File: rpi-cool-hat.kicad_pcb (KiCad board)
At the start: 2 copper layers, 20.3 x 50.8 mm, 3 parts, among them J1 FAN, J2 HAT, J3 RPi

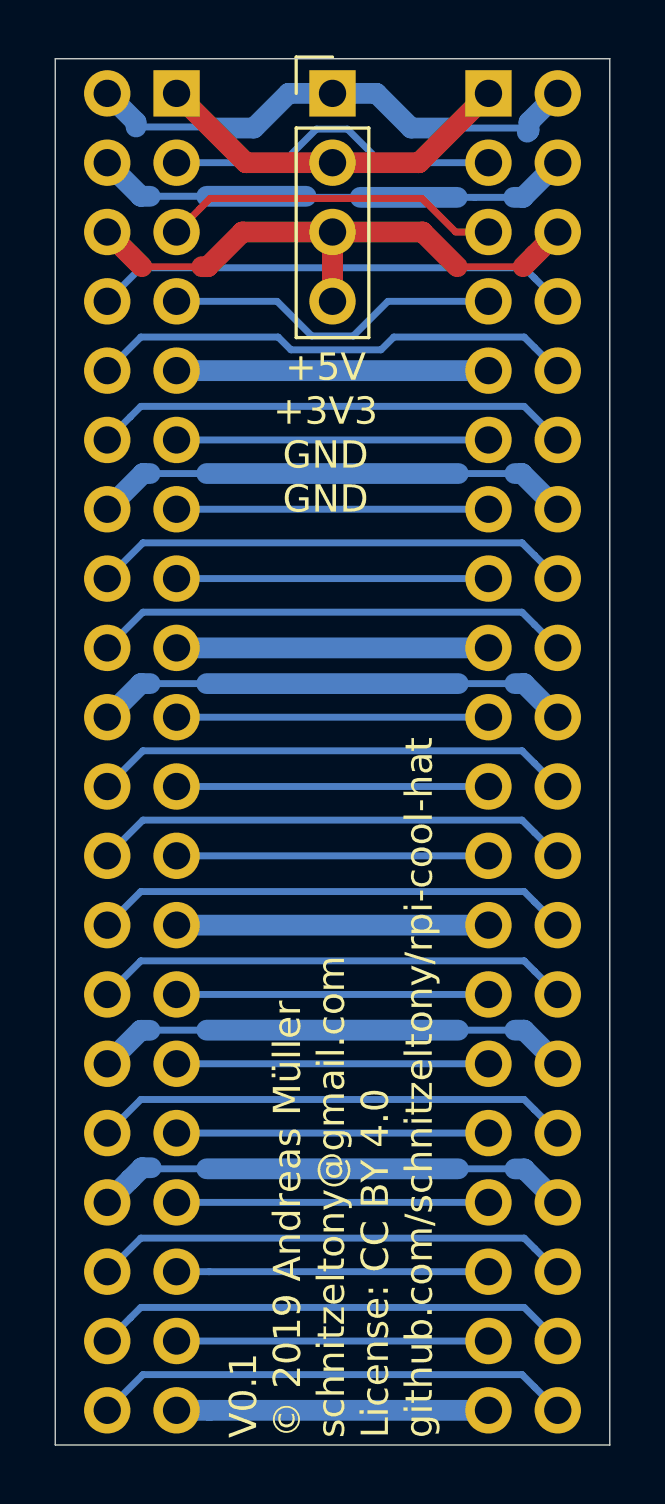
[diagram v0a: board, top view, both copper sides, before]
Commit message: PCB: minor fine tuning on lables and board dimension
Signed-off-by: Andreas Müller <schnitzeltony@gmail.com>
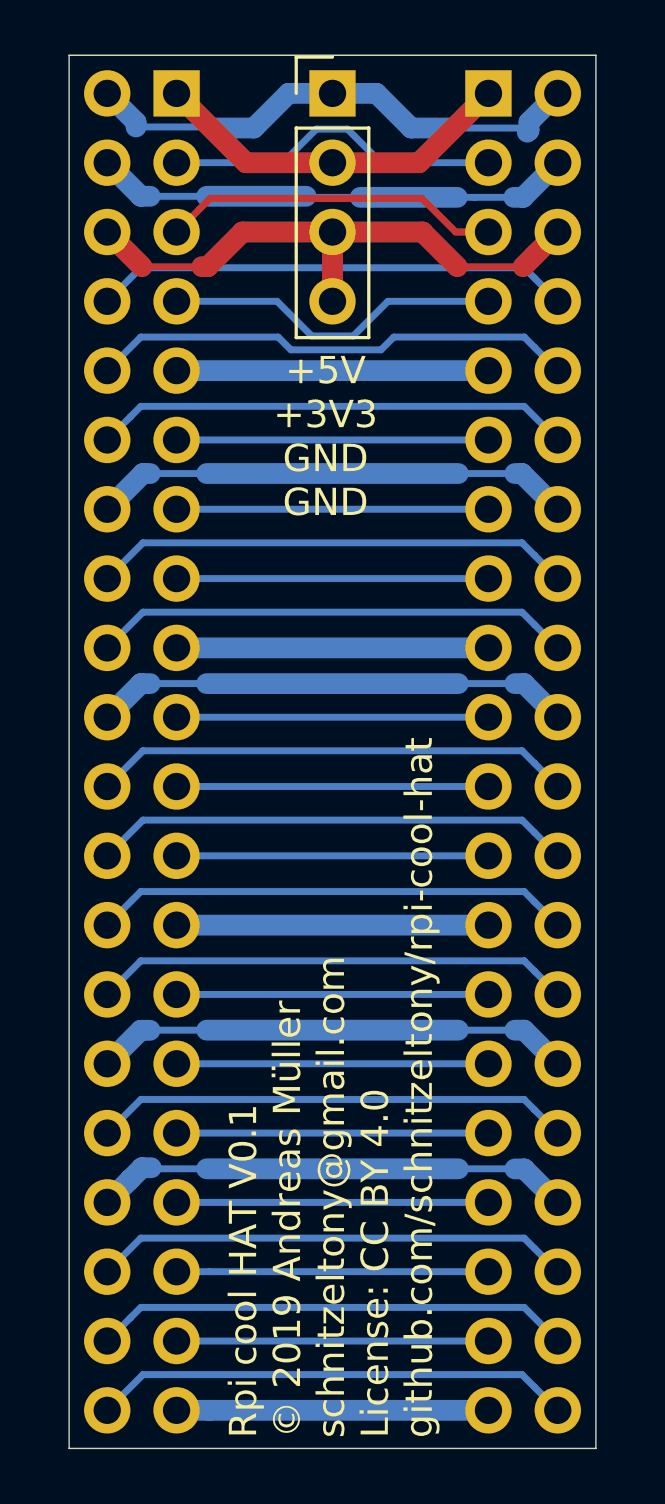
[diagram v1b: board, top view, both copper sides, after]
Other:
- board size 20.3 x 50.8 mm -> 19.3 x 51.1 mm
- board text added: "Rpi cool HAT V0.1 © 2019 Andreas Müller schnitzeltony@gmail.com License: CC BY 4.0 github.com/schnitzeltony/rpi-cool-hat"
- board text removed: "V0.1 © 2019 Andreas Müller schnitzeltony@gmail.com License: CC BY 4.0 github.com/schnitzeltony/rpi-cool-hat"
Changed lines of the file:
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@@
     (descr "Through hole straight pin header, 2x20, 2.54mm pitch, double rows")
     (tags "Through hole pin header THT 2x20 2.54mm double row")
-    (fp_text reference J2 (at -2.159 -23.876 90) (layer F.SilkS) hide
-      (effects (font (size 1 1) (thickness 0.15)))
+    (fp_text reference J2 (at -2.413 -23.876 270) (layer B.SilkS)
+      (effects (font (size 1 1) (thickness 0.15)) (justify mirror))
     )
     (fp_text value HAT (at 1.27 -50.59) (layer B.Fab)
@@
     (descr "Through hole straight pin header, 1x04, 2.54mm pitch, single row")
     (tags "Through hole pin header THT 1x04 2.54mm single row")
-    (fp_text reference J1 (at -1.27 10.16) (layer F.SilkS) hide
-      (effects (font (size 1 1) (thickness 0.15)))
+    (fp_text reference J1 (at 0 10.414 90) (layer B.SilkS)
+      (effects (font (size 1 1) (thickness 0.15)) (justify mirror))
     )
     (fp_text value FAN (at 0 9.95) (layer F.Fab)
@@
     (descr "Through hole straight socket strip, 2x20, 2.54mm pitch, double cols (from Kicad 4.0.7), script generated")
     (tags "Through hole socket strip THT 2x20 2.54mm double row")
-    (fp_text reference J3 (at 1.905 -23.876 90) (layer F.SilkS) hide
-      (effects (font (size 1 1) (thickness 0.15)))
+    (fp_text reference J3 (at 2.413 -23.876 270) (layer B.SilkS)
+      (effects (font (size 1 1) (thickness 0.15)) (justify mirror))
     )
     (fp_text value RPi (at -1.27 -51.03) (layer B.Fab)
@@
     )
   )
-  (gr_text "V0.1\n© 2019 Andreas Müller\nschnitzeltony@gmail.com\nLicense: CC BY 4.0\ngithub.com/schnitzeltony/rpi-cool-hat\n\n" (at 140.462 115.316 90) (layer F.SilkS)
+  (gr_text "Rpi cool HAT V0.1\n© 2019 Andreas Müller\nschnitzeltony@gmail.com\nLicense: CC BY 4.0\ngithub.com/schnitzeltony/rpi-cool-hat\n\n" (at 140.462 115.316 90) (layer F.SilkS)
     (effects (font (size 1 1) (thickness 0.15)) (justify left))
   )
-  (gr_text "+5V\n+3V3\nGND\nGND" (at 139.446 78.486) (layer F.SilkS)
+  (gr_text "+5V\n+3V3\nGND\nGND" (at 139.446 78.613) (layer F.SilkS)
     (effects (font (size 1 1) (thickness 0.15)))
   )
-  (gr_line (start 149.86 115.57) (end 129.54 115.57) (layer Edge.Cuts) (width 0.05))
-  (gr_line (start 149.86 64.77) (end 149.86 115.57) (layer Edge.Cuts) (width 0.05))
-  (gr_line (start 129.54 64.77) (end 149.86 64.77) (layer Edge.Cuts) (width 0.05))
-  (gr_line (start 129.54 115.57) (end 129.54 64.77) (layer Edge.Cuts) (width 0.05))
+  (gr_line (start 149.352 115.697) (end 130.048 115.697) (layer Edge.Cuts) (width 0.05))
+  (gr_line (start 149.352 64.643) (end 149.352 115.697) (layer Edge.Cuts) (width 0.05))
+  (gr_line (start 130.048 64.643) (end 149.352 64.643) (layer Edge.Cuts) (width 0.05))
+  (gr_line (start 130.048 115.697) (end 130.048 64.643) (layer Edge.Cuts) (width 0.05))
   (segment (start 136.525 68.58) (end 139.7 68.58) (width 0.762) (layer F.Cu) (net 1))
   (segment (start 133.985 66.04) (end 136.525 68.58) (width 0.762) (layer F.Cu) (net 1))
